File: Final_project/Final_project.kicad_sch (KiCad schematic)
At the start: 30 parts, among them J1 USB4105-GF-A, U1 RP2040, U2 MCP1702T-3302E_CB, U3 W25Q128JV, Y1 12MHz

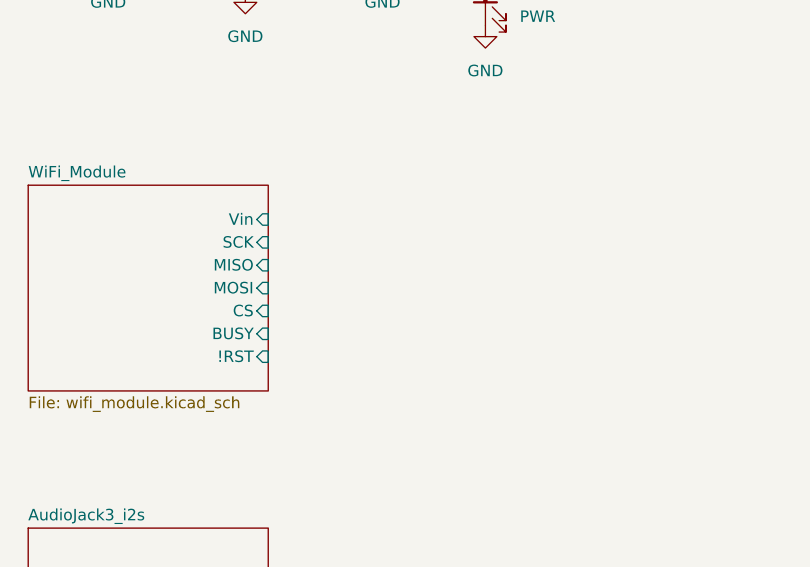
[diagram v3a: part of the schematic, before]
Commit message: Complete pinouts on main
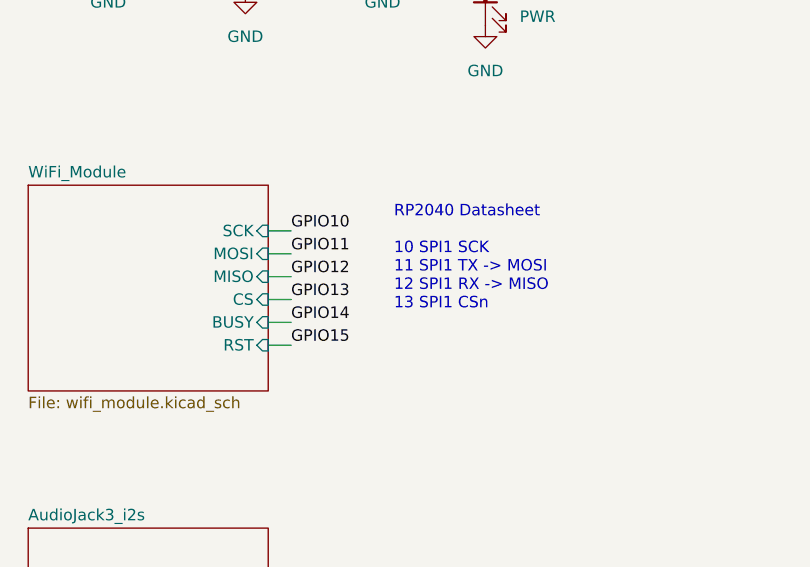
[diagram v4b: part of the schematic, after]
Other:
- sheet WiFi_Module ports: added RST; removed !RST, Vin
- note added: "RP2040 Datasheet 10 SPI1 SCK 11 SPI1 TX -> MOSI 12 SPI1 RX -> MISO 13 SPI1 CSn"
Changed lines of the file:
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@@
+    (stroke (width 0) (type default) (color 0 0 0 0))
+  )
+  (wire (pts (xy 200.66 73.66) (xy 203.2 73.66))
     (stroke (width 0) (type default) (color 0 0 0 0))
   )
@@
     (stroke (width 0) (type default) (color 0 0 0 0))
   )
+  (wire (pts (xy 200.66 78.74) (xy 203.2 78.74))
+    (stroke (width 0) (type default) (color 0 0 0 0))
+  )
   (wire (pts (xy 46.99 49.53) (xy 46.99 50.8))
     (stroke (width 0) (type default) (color 0 0 0 0))
@@
     (stroke (width 0) (type default) (color 0 0 0 0))
   )
+  (wire (pts (xy 200.66 83.82) (xy 203.2 83.82))
+    (stroke (width 0) (type default) (color 0 0 0 0))
+  )
   (wire (pts (xy 66.04 102.87) (xy 86.36 102.87))
     (stroke (width 0) (type default) (color 0 0 0 0))
@@
     (stroke (width 0) (type default) (color 0 0 0 0))
   )
+  (wire (pts (xy 200.66 81.28) (xy 203.2 81.28))
+    (stroke (width 0) (type default) (color 0 0 0 0))
+  )
   (wire (pts (xy 48.26 67.31) (xy 48.26 72.39))
     (stroke (width 0) (type default) (color 0 0 0 0))
@@
     (stroke (width 0) (type default) (color 0 0 0 0))
   )
+  (wire (pts (xy 200.66 86.36) (xy 203.2 86.36))
+    (stroke (width 0) (type default) (color 0 0 0 0))
+  )
   (wire (pts (xy 72.39 168.91) (xy 76.2 168.91))
     (stroke (width 0) (type default) (color 0 0 0 0))
@@
   )
   (wire (pts (xy 72.39 179.07) (xy 72.39 173.99))
+    (stroke (width 0) (type default) (color 0 0 0 0))
+  )
+  (wire (pts (xy 200.66 76.2) (xy 203.2 76.2))
     (stroke (width 0) (type default) (color 0 0 0 0))
   )
@@
     (effects (font (size 1.27 1.27) (thickness 0.254) bold) (justify left bottom))
   )
+  (text "RP2040 Datasheet\n\n10 SPI1 SCK\n11 SPI1 TX -> MOSI\n12 SPI1 RX -> MISO\n13 SPI1 CSn"
+    (at 214.63 82.55 0)
+    (effects (font (size 1.27 1.27)) (justify left bottom))
+  )
   (label "GPIO14" (at 147.32 113.03 0)
     (effects (font (size 1.27 1.27)) (justify left bottom))
@@
     (effects (font (size 1.27 1.27)) (justify left bottom))
   )
+  (label "GPIO13" (at 203.2 81.28 0)
+    (effects (font (size 1.27 1.27)) (justify left bottom))
+  )
   (label "SWCLK" (at 86.36 77.47 180)
     (effects (font (size 1.27 1.27)) (justify right bottom))
@@
     (effects (font (size 1.27 1.27)) (justify left bottom))
   )
+  (label "GPIO11" (at 203.2 76.2 0)
+    (effects (font (size 1.27 1.27)) (justify left bottom))
+  )
   (label "GPIO15" (at 147.32 118.11 0)
     (effects (font (size 1.27 1.27)) (justify left bottom))
   )
+  (label "GPIO15" (at 203.2 86.36 0)
+    (effects (font (size 1.27 1.27)) (justify left bottom))
+  )
   (label "GPIO27" (at 147.32 179.07 0)
     (effects (font (size 1.27 1.27)) (justify left bottom))
@@
     (effects (font (size 1.27 1.27)) (justify left bottom))
   )
+  (label "GPIO10" (at 203.2 73.66 0)
+    (effects (font (size 1.27 1.27)) (justify left bottom))
+  )
   (label "GPIO19" (at 147.32 138.43 0)
     (effects (font (size 1.27 1.27)) (justify left bottom))
@@
   )
   (label "GPIO9" (at 147.32 87.63 0)
+    (effects (font (size 1.27 1.27)) (justify left bottom))
+  )
+  (label "GPIO12" (at 203.2 78.74 0)
     (effects (font (size 1.27 1.27)) (justify left bottom))
   )
@@
   (label "RUN" (at 86.36 87.63 180)
     (effects (font (size 1.27 1.27)) (justify right bottom))
+  )
+  (label "GPIO14" (at 203.2 83.82 0)
+    (effects (font (size 1.27 1.27)) (justify left bottom))
   )
   (label "VBUS" (at 48.26 21.59 0)
@@
       (effects (font (size 1.27 1.27)) hide)
     )
-    (property "Datasheet" "" (id 3) (at 123.19 80.01 0)
+    (property "Datasheet" "https://datasheets.raspberrypi.com/rp2040/rp2040-datasheet.pdf" (id 3) (at 123.19 80.01 0)
       (effects (font (size 1.27 1.27)) hide)
     )
@@
       (effects (font (size 1.27 1.27)) (justify left top))
     )
-    (pin "Vin" input (at 200.66 72.39 0)
-      (effects (font (size 1.27 1.27)) (justify right))
-    )
-    (pin "SCK" input (at 200.66 74.93 0)
-      (effects (font (size 1.27 1.27)) (justify right))
-    )
-    (pin "MISO" input (at 200.66 77.47 0)
-      (effects (font (size 1.27 1.27)) (justify right))
-    )
-    (pin "MOSI" input (at 200.66 80.01 0)
-      (effects (font (size 1.27 1.27)) (justify right))
-    )
-    (pin "CS" input (at 200.66 82.55 0)
-      (effects (font (size 1.27 1.27)) (justify right))
-    )
-    (pin "BUSY" input (at 200.66 85.09 0)
-      (effects (font (size 1.27 1.27)) (justify right))
-    )
-    (pin "!RST" input (at 200.66 87.63 0)
-      (effects (font (size 1.27 1.27)) (justify right))
-    )
+    (pin "SCK" input (at 200.66 73.66 0)
+      (effects (font (size 1.27 1.27)) (justify right))
+    )
+    (pin "MISO" input (at 200.66 78.74 0)
+      (effects (font (size 1.27 1.27)) (justify right))
+    )
+    (pin "MOSI" input (at 200.66 76.2 0)
+      (effects (font (size 1.27 1.27)) (justify right))
+    )
+    (pin "CS" input (at 200.66 81.28 0)
+      (effects (font (size 1.27 1.27)) (justify right))
+    )
+    (pin "BUSY" input (at 200.66 83.82 0)
+      (effects (font (size 1.27 1.27)) (justify right))
+    )
+    (pin "RST" input (at 200.66 86.36 0)
+      (effects (font (size 1.27 1.27)) (justify right))
+    )

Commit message: Add light sensing sheet
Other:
- removed sheet AudioJack3_i2s
- added sheet Light_Sensing (light_sensing.kicad_sch)
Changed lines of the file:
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@@
     (effects (font (size 1.27 1.27)) (justify left bottom))
-  )
-  (hierarchical_label "GPI026" (shape input) (at 199.39 114.3 0)
-    (effects (font (size 1.27 1.27)) (justify left))
-  )
-  (hierarchical_label "GPI028" (shape input) (at 199.39 111.76 0)
-    (effects (font (size 1.27 1.27)) (justify left))
-  )
-  (hierarchical_label "GPI027" (shape input) (at 199.39 116.84 0)
-    (effects (font (size 1.27 1.27)) (justify left))
   )
   (symbol (lib_id "Device:C") (at 80.01 138.43 270) (unit 1)
@@
     )
   )
-  (sheet (at 173.99 106.68) (size 26.67 19.05) (fields_autoplaced)
+  (sheet (at 175.26 100.33) (size 29.21 15.24) (fields_autoplaced)
     (stroke (width 0.1524) (type solid) (color 0 0 0 0))
     (fill (color 255 255 194 1.0000))
-    (property "Sheet name" "AudioJack3_i2s" (id 0) (at 173.99 105.9684 0)
+    (property "Sheet name" "Light_Sensing" (id 0) (at 175.26 99.6184 0)
       (effects (font (size 1.27 1.27)) (justify left bottom))
     )
-    (property "Sheet file" "audiojack.kicad_sch" (id 1) (at 173.99 126.3146 0)
+    (property "Sheet file" "light_sensing.kicad_sch" (id 1) (at 175.26 116.1546 0)
       (effects (font (size 1.27 1.27)) (justify left top))
     )
@@
     (path "/" (page "1"))
     (path "/5f380518-a4aa-4cf5-aa47-79ba18474bc7" (page "2"))
-    (path "/a587f9f9-6d27-4989-a344-d47a4b55e4be" (page "3"))
+    (path "/9044928e-cf49-4703-b68a-b82a255f3d2f" (page "3"))
   )
   (symbol_instances
@@
       (reference "#PWR0136") (unit 1) (value "+3.3V") (footprint "")
     )
-    (path "/a587f9f9-6d27-4989-a344-d47a4b55e4be/c5d9e064-0af4-4e0e-bd6b-664c26893538"
-      (reference "#PWR0137") (unit 1) (value "GND") (footprint "")
-    )
-    (path "/a587f9f9-6d27-4989-a344-d47a4b55e4be/1201ed2b-c83a-4076-ab82-b86ccf22e2d8"
-      (reference "#PWR0138") (unit 1) (value "GND") (footprint "")
-    )
-    (path "/a587f9f9-6d27-4989-a344-d47a4b55e4be/f777ab7c-e6a7-4864-a1b4-ecf9b8ca83a6"
-      (reference "#PWR0139") (unit 1) (value "GND") (footprint "")
-    )
-    (path "/a587f9f9-6d27-4989-a344-d47a4b55e4be/9c73f79e-72f2-441d-9dac-3a76166cfc0f"
-      (reference "#PWR0140") (unit 1) (value "GND") (footprint "")
-    )
-    (path "/a587f9f9-6d27-4989-a344-d47a4b55e4be/e7bca9cb-56d9-40d7-b52c-98f8ee37531b"
-      (reference "#PWR0141") (unit 1) (value "+3.3V") (footprint "")
-    )
-    (path "/a587f9f9-6d27-4989-a344-d47a4b55e4be/b29c74a1-5507-43c7-b407-6f553b561306"
-      (reference "#PWR0142") (unit 1) (value "+3.3VA") (footprint "")
-    )
-    (path "/a587f9f9-6d27-4989-a344-d47a4b55e4be/c6485d7e-2f99-424a-8892-8c156e29ea1e"
-      (reference "#PWR0143") (unit 1) (value "GND") (footprint "")
-    )
-    (path "/a587f9f9-6d27-4989-a344-d47a4b55e4be/39d40543-4640-4cd0-b3bb-ff63afad37e6"
-      (reference "#PWR0144") (unit 1) (value "+3.3V") (footprint "")
-    )
-    (path "/a587f9f9-6d27-4989-a344-d47a4b55e4be/b77c1d5b-da62-4aeb-86fe-245da2ab1142"
-      (reference "#PWR0145") (unit 1) (value "GND") (footprint "")
-    )
-    (path "/a587f9f9-6d27-4989-a344-d47a4b55e4be/7e4dd788-7a5d-498c-a355-c25173e9bece"
-      (reference "#PWR0146") (unit 1) (value "GND") (footprint "")
-    )
-    (path "/a587f9f9-6d27-4989-a344-d47a4b55e4be/86636571-fe92-4ced-bb1d-a8fcfd911d5a"
-      (reference "#PWR0147") (unit 1) (value "GND") (footprint "")
-    )
-    (path "/a587f9f9-6d27-4989-a344-d47a4b55e4be/e5df6f56-153a-4058-a192-53505e63ff38"
-      (reference "#PWR0148") (unit 1) (value "GND") (footprint "")
-    )
-    (path "/a587f9f9-6d27-4989-a344-d47a4b55e4be/ec4215f0-1fe5-4d10-b099-92e2be274524"
-      (reference "#PWR0149") (unit 1) (value "GND") (footprint "")
-    )
     (path "/4185e825-d3db-49f7-84c3-1d674f768766"
       (reference "C1") (unit 1) (value "0.1µF") (footprint "Final_project:CL10B104JB8NNNC")
@@
       (reference "C16") (unit 1) (value "10µF") (footprint "Final_project:GRM188R61E106KA73D")
     )
-    (path "/a587f9f9-6d27-4989-a344-d47a4b55e4be/89decb5b-5a9b-4b31-a61b-8249c0836c65"
-      (reference "C17") (unit 1) (value "10µF") (footprint "Final_project:GRM188R61E106KA73D")
-    )
-    (path "/a587f9f9-6d27-4989-a344-d47a4b55e4be/fbd1a9a6-59f5-45de-b4fb-5d8cbe0d06ec"
-      (reference "C18") (unit 1) (value "0.1µF") (footprint "Final_project:CL10B104JB8NNNC")
-    )
-    (path "/a587f9f9-6d27-4989-a344-d47a4b55e4be/2d0b1a2c-4c48-403a-b726-4304a7fba6c2"
-      (reference "C19") (unit 1) (value "0.1µF") (footprint "Final_project:CL10B104JB8NNNC")
-    )
-    (path "/a587f9f9-6d27-4989-a344-d47a4b55e4be/eab518e2-1795-4e04-bca7-e5f94ae08054"
-      (reference "C20") (unit 1) (value "2.2u") (footprint "Capacitor_SMD:C_0603_1608Metric")
-    )
-    (path "/a587f9f9-6d27-4989-a344-d47a4b55e4be/0b581dd4-3c54-4ed2-bc9f-a0dc6376e54f"
-      (reference "C21") (unit 1) (value "10µF") (footprint "Final_project:GRM188R61E106KA73D")
-    )
-    (path "/a587f9f9-6d27-4989-a344-d47a4b55e4be/d1fa018d-a46d-4b03-888f-95138aee8531"
-      (reference "C22") (unit 1) (value "2.2u") (footprint "Capacitor_SMD:C_0603_1608Metric")
-    )
-    (path "/a587f9f9-6d27-4989-a344-d47a4b55e4be/5e934f0e-0761-4578-8dc4-68ea01f703f2"
-      (reference "C23") (unit 1) (value "0.1µF") (footprint "Final_project:CL10B104JB8NNNC")
-    )
-    (path "/a587f9f9-6d27-4989-a344-d47a4b55e4be/7071c17c-5b29-4188-91a8-a2e24199fb05"
-      (reference "C24") (unit 1) (value "0.1µF") (footprint "Final_project:CL10B104JB8NNNC")
-    )
-    (path "/a587f9f9-6d27-4989-a344-d47a4b55e4be/28faf2b6-5367-4581-9929-d819ff1b116c"
-      (reference "C25") (unit 1) (value "10µF") (footprint "Final_project:GRM188R61E106KA73D")
-    )
-    (path "/a587f9f9-6d27-4989-a344-d47a4b55e4be/55fc7409-cc0b-4ac6-ac8a-8110bbe93f23"
-      (reference "C26") (unit 1) (value "2.2n") (footprint "Capacitor_SMD:C_0402_1005Metric")
-    )
-    (path "/a587f9f9-6d27-4989-a344-d47a4b55e4be/281907a1-0f61-4462-9844-50f9c6f52a6e"
-      (reference "C27") (unit 1) (value "2.2n") (footprint "Capacitor_SMD:C_0402_1005Metric")
-    )
     (path "/c2461336-3de5-4651-bacc-5ee03cccd9eb"
       (reference "D1") (unit 1) (value "LED") (footprint "Final_project:LTST-C170TBKT")
@@
       (reference "J1") (unit 1) (value "USB4105-GF-A") (footprint "Final_project:USB4105-GF-A")
     )
-    (path "/a587f9f9-6d27-4989-a344-d47a4b55e4be/9749586b-6f71-4301-b771-984410f8fabe"
-      (reference "J2") (unit 1) (value "AudioJack3") (footprint "Connector_Audio:Jack_3.5mm_Lumberg_1503_07_Horizontal")
-    )
     (path "/6e52ec09-aa2b-4fd4-928b-f8255f408a1b"
       (reference "R1") (unit 1) (value "5.1K") (footprint "Final_project:RES_ERJ3EKF5101V")
@@
       (reference "R13") (unit 1) (value "1K") (footprint "Final_project:RC0603FR-071KL")
     )
-    (path "/a587f9f9-6d27-4989-a344-d47a4b55e4be/a661dc1d-80d2-4992-a1b5-c31ce823226b"
-      (reference "R14") (unit 1) (value "470") (footprint "Resistor_SMD:R_0402_1005Metric")
-    )
-    (path "/a587f9f9-6d27-4989-a344-d47a4b55e4be/891f254e-0e9c-4422-b902-5506d77704e1"
-      (reference "R15") (unit 1) (value "470") (footprint "Resistor_SMD:R_0402_1005Metric")
-    )
     (path "/d88ecd80-f389-40aa-8f67-79097bb2830a"
       (reference "S1") (unit 1) (value "RST") (footprint "Final_project:KXT321LHS")
@@
       (reference "U4") (unit 1) (value "ESP32-WROOM-32") (footprint "Final_project:MODULE_ESP32-WROOM-32")
     )
-    (path "/a587f9f9-6d27-4989-a344-d47a4b55e4be/75e165d3-0338-43dd-b063-e35fba705dac"
-      (reference "U5") (unit 1) (value "PCM5101A") (footprint "Package_SO:TSSOP-20_4.4x6.5mm_P0.65mm")
-    )
     (path "/b995bef3-23bd-41bd-824d-90a30eae13e1"

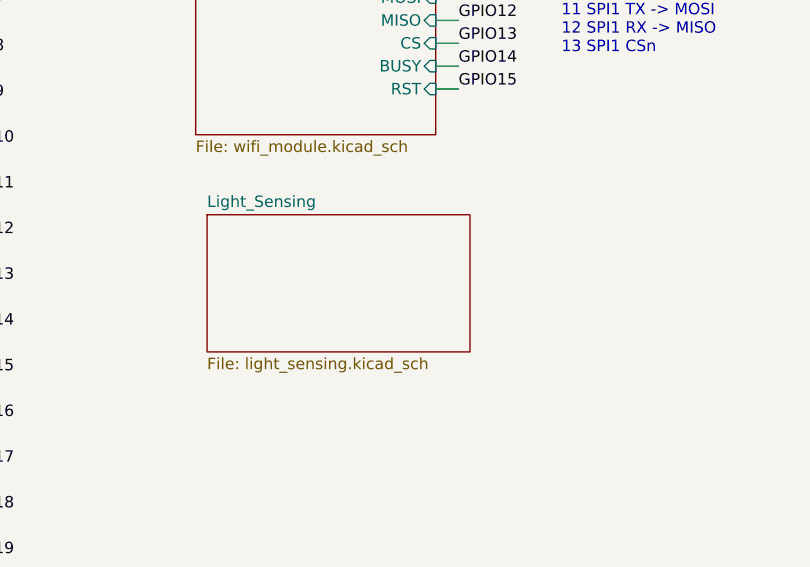
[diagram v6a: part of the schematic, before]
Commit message: Add miniproj parts, begin photosensing circuit
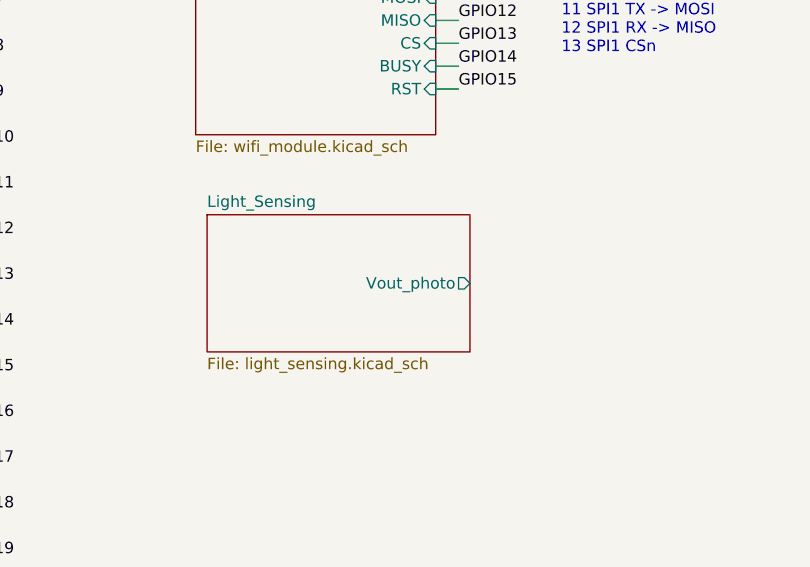
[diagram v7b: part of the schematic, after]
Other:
- sheet Light_Sensing ports: added Vout_photo; removed none
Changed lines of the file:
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@@
       (effects (font (size 1.27 1.27)) (justify left top))
+    )
+    (pin "Vout_photo" output (at 204.47 107.95 0)
+      (effects (font (size 1.27 1.27)) (justify right))
     )
   )
@@
       (reference "#PWR0136") (unit 1) (value "+3.3V") (footprint "")
     )
+    (path "/9044928e-cf49-4703-b68a-b82a255f3d2f/6dca002b-3689-4d76-ba7e-971dd354462d"
+      (reference "#PWR?") (unit 1) (value "GND") (footprint "")
+    )
+    (path "/9044928e-cf49-4703-b68a-b82a255f3d2f/ce0c8187-9534-4154-9f98-3cba46857436"
+      (reference "#PWR?") (unit 1) (value "+3V3") (footprint "")
+    )
     (path "/4185e825-d3db-49f7-84c3-1d674f768766"
       (reference "C1") (unit 1) (value "0.1µF") (footprint "Final_project:CL10B104JB8NNNC")
@@
       (reference "C16") (unit 1) (value "10µF") (footprint "Final_project:GRM188R61E106KA73D")
     )
+    (path "/9044928e-cf49-4703-b68a-b82a255f3d2f/a8f6fea5-6a80-4abe-adc8-0fd7cd1d1516"
+      (reference "C?") (unit 1) (value "C") (footprint "")
+    )
     (path "/c2461336-3de5-4651-bacc-5ee03cccd9eb"
       (reference "D1") (unit 1) (value "LED") (footprint "Final_project:LTST-C170TBKT")
@@
       (reference "D5") (unit 1) (value "LED") (footprint "Final_project:LTST-C170TBKT")
     )
+    (path "/9044928e-cf49-4703-b68a-b82a255f3d2f/1736b8b7-6bdb-41af-8ad7-83d4bf1750af"
+      (reference "D?") (unit 1) (value "D_Photo") (footprint "")
+    )
     (path "/153205ff-d08c-4a78-91d6-71b25838037b"
       (reference "J1") (unit 1) (value "USB4105-GF-A") (footprint "Final_project:USB4105-GF-A")
@@
       (reference "R13") (unit 1) (value "1K") (footprint "Final_project:RC0603FR-071KL")
     )
+    (path "/9044928e-cf49-4703-b68a-b82a255f3d2f/0aea6349-0e56-48d6-87a8-964bdf7f3177"
+      (reference "R?") (unit 1) (value "R") (footprint "")
+    )
     (path "/d88ecd80-f389-40aa-8f67-79097bb2830a"
       (reference "S1") (unit 1) (value "RST") (footprint "Final_project:KXT321LHS")
@@
       (reference "U4") (unit 1) (value "ESP32-WROOM-32") (footprint "Final_project:MODULE_ESP32-WROOM-32")
     )
+    (path "/9044928e-cf49-4703-b68a-b82a255f3d2f/0db1a1ec-8c01-4b3e-9b95-87118412500d"
+      (reference "U?") (unit 1) (value "MCP6021T-E_OT") (footprint "Package_TO_SOT_SMD:SOT-23-5")
+    )
     (path "/b995bef3-23bd-41bd-824d-90a30eae13e1"

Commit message: started layout
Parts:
- added J2: Conn_01x04, Connector_PinSocket_2.54mm:PinSocket_1x04_P2.54mm_Horizontal, symbol Connector_Generic:Conn_01x04
- added J3: DEBUG, Connector_PinSocket_2.54mm:PinSocket_1x03_P2.54mm_Vertical, symbol Connector_Generic:Conn_01x03
- added J4: LEFT, Connector_PinSocket_2.54mm:PinSocket_1x20_P2.54mm_Vertical, symbol Connector_Generic:Conn_01x20
- added J5: RIGHT, Connector_PinSocket_2.54mm:PinSocket_1x20_P2.54mm_Vertical, symbol Connector_Generic:Conn_01x20
- U2: footprint MP1:MCP1702T-3302E&slash_CB -> Final_project:MCP1702T-3302E&slash_CB
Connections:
- net +3V3: now also J5.5 (Pin_5)
- net BOOT: now also J5.4 (Pin_4)
- net GND: now also J2.4 (Pin_4), J3.2 (Pin_2), J4.13 (Pin_13), J4.18 (Pin_18), J4.3 (Pin_3), J4.8 (Pin_8), J5.13 (Pin_13), J5.18 (Pin_18), J5.3 (Pin_3), J5.8 (Pin_8)
- net GPIO0: now also J4.1 (Pin_1)
- net GPIO1: now also J4.2 (Pin_2)
- net GPIO10: now also J4.14 (Pin_14)
- net GPIO11: now also J4.15 (Pin_15)
- net GPIO12: now also J4.16 (Pin_16)
- net GPIO13: now also J4.17 (Pin_17)
- net GPIO14: now also J4.19 (Pin_19)
- net GPIO15: now also J4.20 (Pin_20)
- net GPIO16: now also J5.20 (Pin_20)
- net GPIO17: now also J5.19 (Pin_19)
- net GPIO18: now also J5.17 (Pin_17)
- net GPIO19: now also J5.16 (Pin_16)
- net GPIO2: now also J2.2 (Pin_2), J4.4 (Pin_4)
- net GPIO20: now also J5.15 (Pin_15)
- net GPIO21: now also J5.14 (Pin_14)
- net GPIO22: now also J5.12 (Pin_12)
- net GPIO23: now also J5.2 (Pin_2)
- net GPIO26: now also J5.10 (Pin_10)
- net GPIO27: now also J5.9 (Pin_9)
- net GPIO28: now also J5.7 (Pin_7)
- net GPIO29: now also J5.6 (Pin_6)
- net GPIO3: now also J2.1 (Pin_1), J4.5 (Pin_5)
- net GPIO4: now also J4.6 (Pin_6)
- net GPIO5: now also J4.7 (Pin_7)
- net GPIO6: now also J4.9 (Pin_9)
- net GPIO7: now also J4.10 (Pin_10)
- net GPIO8: now also J4.11 (Pin_11)
- net GPIO9: now also J4.12 (Pin_12)
- net RUN: now also J5.11 (Pin_11)
- net SWCLK: now also J3.1 (Pin_1)
- net SWDIO: now also J3.3 (Pin_3)
- net VBUS: now also J2.3 (Pin_3), J5.1 (Pin_1)
- no-connect marks 2 -> 3
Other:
- sheet Light_Sensing ports: added AO, DO; removed Vout_photo
- note added: "Connect to Screen (I2C)"
- note added: "Horizontal Connector"
- moved on the sheet: C12, C13, D2, R8, U2
